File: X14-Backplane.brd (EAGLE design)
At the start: 160 x 100 mm, 28 parts, among them J2 PXC-PTSM-04-RA-1778641, J3 PXC-8-RA-1778683, J7 POE_TERMINAL

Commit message: X14-Backplane 11/29
This is the most up to date backplane as of 11/29/2021
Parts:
- removed C5: 47uF, Panasonic 47 uF cap - EEE-1CA470SP:PANASONIC_D
- removed J7: POE_TERMINAL, Dist_POE:CONN2_282834-2_TEC
- added J8: PXC-8-RA-1778683, Phoenix Contact PTSM 8 pin:PXC-8-RA-1778683
- added U$9: IPL_13X2, PI-SHIELD, Solenoid-Backplane:IPL13X2
- U$4: device CONN, Distribution-Backplane:IPL1-106-01-L-D-K(B-D) -> CONN, Distribution-Backplane:SAMTEC_IPL1-107-01-X-D-K(B-D)
- moved U$1 20.4 mm to (-100.3, 104.1), turned to 180 degrees
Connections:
- new net +3V3: U$9.1
- new net ALERT1: U$9.17
- new net ALERT2: U$9.19
- new net SOL1_1: J8.8, U$9.8
- new net SOL2_1: J8.7, U$9.10
- new net SOL3_1: J8.6, U$9.12
- new net SOL4_1: J8.5, U$9.14
- new net SOL5_1: J8.4, U$9.16
- new net SOL6_1: J8.3, U$9.18
- new net SWCLK: U$9.11
- new net SWDIO: U$9.13
- net 12V: now also J8.1, J8.2, U$4.07, U$9.2; no longer C5.+
- net 3V3: now also U$4.04; no longer U$4.4
- net 5V: now also U$4.01, U$4.02, U$4.03, U$9.3; no longer J7.1, U$4.1, U$4.2, U$4.3
- net ALERT_1: now also U$4.09; no longer U$4.8
- net ALERT_2: now also U$4.10; no longer U$4.9
- net C2_1: now also U$4.12, U$9.21; no longer U$4.11
- net C2_2: now also U$4.13, U$9.22; no longer U$4.12
- net CAN_H: now also U$9.24
- net CAN_L: now also U$9.26
- net CLK: now also U$4.11, U$9.23; no longer U$4.10
- net DATA: now also U$4.08, U$9.25; no longer U$4.7
- net GND: now also U$4.05, U$4.06, U$9.15, U$9.20, U$9.4, U$9.5, U$9.6, U$9.7, U$9.9; no longer C5.-, J7.2, U$4.5, U$4.6
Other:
- board size 160 x 100 mm -> 88.9 x 139.7 mm

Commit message: X14-Backplane 12/2
Most up to date backplane as of 12/2/2021
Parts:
- U$9: value IPL_13X2 -> 6X_CONN; device PI-SHIELD, Solenoid-Backplane:IPL13X2 -> PI-SHIELD, Solenoid-Backplane:IPL6X2
- moved R9 254.0 mm to (85.6, 28.7), turned to 180 degrees
- moved U$4 248.7 mm to (82.5, 123.4), turned to 270 degrees
- moved J8 246.2 mm to (86.1, 83.3), turned to 90 degrees
- moved U$5 245.0 mm to (95.2, 128.3), turned to 180 degrees
- moved J2 237.2 mm to (70.9, 50.8)
- moved J3 233.7 mm to (86.4, 59.2), turned to 90 degrees
- moved D4 232.9 mm to (85.6, 26.2), turned to 180 degrees
- moved D3 229.1 mm to (85.6, 23.4), turned to 180 degrees
- moved D2 225.6 mm to (85.6, 20.6), turned to 180 degrees
- moved R8 225.1 mm to (72.6, 54.9), turned to 90 degrees
- moved U$9 225.1 mm to (74.7, 88.1), turned to 90 degrees
- moved R7 224.3 mm to (75.4, 54.9), turned to 270 degrees
- moved H2 223.0 mm to (85.1, 3.81), flipped to the bottom
- moved D1 222.3 mm to (85.6, 17.8), turned to 180 degrees
- moved R5 215.2 mm to (26.7, 11.4), turned to 180 degrees
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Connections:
- removed net +3V3: U$9.1
- removed net ALERT1: U$9.17
- removed net ALERT2: U$9.19
- removed net GND: C4.2, J2.1, J3.1, J6.4, MUX.6, MUX.7, MUX.8, R1.1, R4.1, R5.1, U$1.10, U$2.10, U$3.10, U$4.05, U$4.06, U$8.1, U$9.15, U$9.20, U$9.4, U$9.5, U$9.6, U$9.7, U$9.9
- removed net SWCLK: U$9.11
- removed net SWDIO: U$9.13
- new net 12V_L: J8.1, J8.2, U$4.07, U$9.1, U$9.3
- new net GND_L: C4.2, J2.1, J3.1, J6.4, MUX.6, MUX.7, MUX.8, R1.1, R4.1, R5.1, U$1.10, U$2.10, U$3.10, U$4.14, U$8.1, U$9.5, U$9.9
- new net JH: U$4.05, U$4.06
- net 12V: no longer J8.1, J8.2, U$4.07, U$9.2
- net 3V3: now also U$9.11
- net 5V: now also U$9.7; no longer U$9.3
- net C2_1: no longer U$9.21
- net C2_2: no longer U$9.22
- net CAN_H: no longer U$9.24
- net CAN_L: no longer U$9.26
- net CLK: no longer U$9.23
- net DATA: no longer U$9.25
- net SOL1_1: now also J8.3, U$9.2; no longer J8.8, U$9.8
- net SOL2_1: now also J8.4, U$9.4; no longer J8.7, U$9.10
- net SOL3_1: now also J8.5, U$9.6; no longer J8.6, U$9.12
- net SOL4_1: now also J8.6, U$9.8; no longer J8.5, U$9.14
- net SOL5_1: now also J8.7, U$9.10; no longer J8.4, U$9.16
- net SOL6_1: now also J8.8, U$9.12; no longer J8.3, U$9.18
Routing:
- net CAN_L: track 0.00 -> 146.4 mm, vias 0 -> 2
- net CAN_H: track 0.00 -> 130.8 mm
- net SWCLK_3: track 0.00 -> 109.8 mm, vias 0 -> 1
- net SWDIO_3: track 0.00 -> 109.2 mm, vias 0 -> 1
- net NRST_3: track 0.00 -> 82.0 mm, vias 0 -> 1
- net SWCLK_2: track 0.00 -> 68.0 mm, vias 0 -> 1
- net SWDIO_2: track 0.00 -> 62.0 mm, vias 0 -> 1
- net 12V_L: track 0.00 -> 49.0 mm
- net C2_2: track 0.00 -> 29.8 mm
- net 5V: track 0.00 -> 28.1 mm
- net 3V3: track 0.00 -> 25.9 mm, vias 0 -> 2
- net C2_1: track 0.00 -> 25.8 mm
- net CLK: track 0.00 -> 21.8 mm
- net ALERT_2: track 0.00 -> 17.9 mm
- net PROG_1: track 0.00 -> 16.7 mm
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- added copper zone on layer 16, net 3V3
- added copper zone on layer 1, net 5V
- added copper zone on layer 1, net GND_L
- added copper zone on layer 16, net GND_L
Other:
- board size 88.9 x 139.7 mm -> 88.9 x 140.2 mm
- board text added: "Reserved Space for SMBUS->I2C Board"

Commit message: sfdgfhg
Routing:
- net NRST_3: track 82.0 -> 75.3 mm
- net SWDIO_2: track 62.0 -> 63.4 mm
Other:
- board text added: "Reserved Space for SMBUS->CAN Board"
- board text removed: "Reserved Space for SMBUS->I2C Board"
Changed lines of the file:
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@@
 <wire x1="38.862" y1="-0.508" x2="38.862" y2="1.016" width="0.1524" layer="46"/>
 <text x="67.818" y="123.952" size="1.016" layer="125">Reserved Space
-for SMBUS-&gt;I2C
+for SMBUS-&gt;CAN
 Board</text>
 </plain>
@@
 <contactref element="U$2" pad="9"/>
 <wire x1="20.78" y1="56.372" x2="20.78" y2="59.388" width="0.1524" layer="16"/>
-<wire x1="64.516" y1="72.136" x2="67.564" y2="75.184" width="0.1524" layer="16"/>
+<wire x1="65.532" y1="73.152" x2="67.564" y2="75.184" width="0.1524" layer="16"/>
 <via x="67.564" y="75.184" extent="1-16" drill="0.35"/>
-<wire x1="20.78" y1="59.388" x2="23.622" y2="62.23" width="0.1524" layer="16"/>
-<wire x1="23.622" y1="62.23" x2="61.722" y2="62.23" width="0.1524" layer="16"/>
-<wire x1="61.722" y1="62.23" x2="64.516" y2="65.024" width="0.1524" layer="16"/>
-<wire x1="64.516" y1="65.024" x2="64.516" y2="72.136" width="0.1524" layer="16"/>
+<wire x1="20.78" y1="59.388" x2="22.86" y2="61.468" width="0.1524" layer="16"/>
+<wire x1="22.86" y1="61.468" x2="63.246" y2="61.468" width="0.1524" layer="16"/>
+<wire x1="63.246" y1="61.468" x2="65.532" y2="63.754" width="0.1524" layer="16"/>
+<wire x1="65.532" y1="63.754" x2="65.532" y2="73.152" width="0.1524" layer="16"/>
 <wire x1="67.564" y1="75.184" x2="69.088" y2="75.184" width="0.1524" layer="1"/>
 </signal>
@@
 <contactref element="U$2" pad="11"/>
 <wire x1="22.78" y1="56.372" x2="22.78" y2="59.102" width="0.1524" layer="16"/>
-<wire x1="24.384" y1="60.706" x2="62.738" y2="60.706" width="0.1524" layer="16"/>
-<wire x1="62.738" y1="60.706" x2="66.04" y2="64.008" width="0.1524" layer="16"/>
-<wire x1="66.04" y1="64.008" x2="66.04" y2="72.644" width="0.1524" layer="16"/>
-<wire x1="66.04" y1="72.644" x2="67.056" y2="73.66" width="0.1524" layer="16"/>
+<wire x1="24.384" y1="60.706" x2="63.5" y2="60.706" width="0.1524" layer="16"/>
+<wire x1="63.5" y1="60.706" x2="66.294" y2="63.5" width="0.1524" layer="16"/>
+<wire x1="66.294" y1="63.5" x2="66.294" y2="72.898" width="0.1524" layer="16"/>
+<wire x1="66.294" y1="72.898" x2="67.056" y2="73.66" width="0.1524" layer="16"/>
 <wire x1="70.866" y1="73.66" x2="71.628" y2="74.422" width="0.1524" layer="16"/>
 <wire x1="71.628" y1="74.422" x2="71.628" y2="76.2" width="0.1524" layer="16"/>
@@
 <wire x1="22.78" y1="15.922" x2="24.384" y2="17.526" width="0.1524" layer="16"/>
 <wire x1="24.384" y1="17.526" x2="59.944" y2="17.526" width="0.1524" layer="16"/>
-<wire x1="61.976" y1="19.558" x2="61.976" y2="55.118" width="0.1524" layer="16"/>
+<wire x1="61.976" y1="19.558" x2="61.976" y2="56.642" width="0.1524" layer="16"/>
 <via x="75.692" y="77.978" extent="1-16" drill="0.35"/>
 <wire x1="75.692" y1="77.978" x2="75.692" y2="78.232" width="0.1524" layer="1"/>
 <wire x1="75.692" y1="78.232" x2="74.93" y2="78.994" width="0.1524" layer="1"/>
 <wire x1="74.93" y1="78.994" x2="73.768" y2="78.994" width="0.1524" layer="1"/>
-<wire x1="61.976" y1="55.118" x2="75.692" y2="68.834" width="0.1524" layer="16"/>
-<wire x1="75.692" y1="68.834" x2="75.692" y2="77.978" width="0.1524" layer="16"/>
+<wire x1="61.976" y1="56.642" x2="75.692" y2="70.358" width="0.1524" layer="16"/>
+<wire x1="75.692" y1="70.358" x2="75.692" y2="77.978" width="0.1524" layer="16"/>
 </signal>
 <signal name="CAN_H">
@@
 <contactref element="D3" pad="A"/>
 <contactref element="U$3" pad="6"/>
-<wire x1="16.78" y1="11.446" x2="16.78" y2="9.128" width="0.1524" layer="16"/>
-<wire x1="16.78" y1="9.128" x2="18.288" y2="7.62" width="0.1524" layer="16"/>
-<wire x1="18.288" y1="7.62" x2="66.294" y2="7.62" width="0.1524" layer="16"/>
-<wire x1="68.326" y1="9.652" x2="68.326" y2="18.034" width="0.1524" layer="16"/>
-<wire x1="68.326" y1="18.034" x2="73.66" y2="23.368" width="0.1524" layer="16"/>
-<wire x1="66.294" y1="7.62" x2="68.326" y2="9.652" width="0.1524" layer="16"/>
+<wire x1="16.78" y1="11.446" x2="16.78" y2="10.144" width="0.1524" layer="16"/>
+<wire x1="16.78" y1="10.144" x2="17.78" y2="9.144" width="0.1524" layer="16"/>
+<wire x1="17.78" y1="9.144" x2="59.436" y2="9.144" width="0.1524" layer="16"/>
+<wire x1="59.436" y1="9.144" x2="73.66" y2="23.368" width="0.1524" layer="16"/>
 <wire x1="73.66" y1="23.368" x2="78.232" y2="23.368" width="0.1524" layer="16"/>
 <via x="78.232" y="23.368" extent="1-16" drill="0.35"/>

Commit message: Revert "sfdgfhg"
This reverts commit 89fcb60d7aa2de489dc8c4b854d40a80c75a218c.
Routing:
- net NRST_3: track 75.3 -> 82.0 mm
- net SWDIO_2: track 63.4 -> 62.0 mm
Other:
- board text added: "Reserved Space for SMBUS->I2C Board"
- board text removed: "Reserved Space for SMBUS->CAN Board"
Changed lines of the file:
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@@
 <wire x1="38.862" y1="-0.508" x2="38.862" y2="1.016" width="0.1524" layer="46"/>
 <text x="67.818" y="123.952" size="1.016" layer="125">Reserved Space
-for SMBUS-&gt;CAN
+for SMBUS-&gt;I2C
 Board</text>
 </plain>
@@
 <contactref element="U$2" pad="9"/>
 <wire x1="20.78" y1="56.372" x2="20.78" y2="59.388" width="0.1524" layer="16"/>
-<wire x1="65.532" y1="73.152" x2="67.564" y2="75.184" width="0.1524" layer="16"/>
+<wire x1="64.516" y1="72.136" x2="67.564" y2="75.184" width="0.1524" layer="16"/>
 <via x="67.564" y="75.184" extent="1-16" drill="0.35"/>
-<wire x1="20.78" y1="59.388" x2="22.86" y2="61.468" width="0.1524" layer="16"/>
-<wire x1="22.86" y1="61.468" x2="63.246" y2="61.468" width="0.1524" layer="16"/>
-<wire x1="63.246" y1="61.468" x2="65.532" y2="63.754" width="0.1524" layer="16"/>
-<wire x1="65.532" y1="63.754" x2="65.532" y2="73.152" width="0.1524" layer="16"/>
+<wire x1="20.78" y1="59.388" x2="23.622" y2="62.23" width="0.1524" layer="16"/>
+<wire x1="23.622" y1="62.23" x2="61.722" y2="62.23" width="0.1524" layer="16"/>
+<wire x1="61.722" y1="62.23" x2="64.516" y2="65.024" width="0.1524" layer="16"/>
+<wire x1="64.516" y1="65.024" x2="64.516" y2="72.136" width="0.1524" layer="16"/>
 <wire x1="67.564" y1="75.184" x2="69.088" y2="75.184" width="0.1524" layer="1"/>
 </signal>
@@
 <contactref element="U$2" pad="11"/>
 <wire x1="22.78" y1="56.372" x2="22.78" y2="59.102" width="0.1524" layer="16"/>
-<wire x1="24.384" y1="60.706" x2="63.5" y2="60.706" width="0.1524" layer="16"/>
-<wire x1="63.5" y1="60.706" x2="66.294" y2="63.5" width="0.1524" layer="16"/>
-<wire x1="66.294" y1="63.5" x2="66.294" y2="72.898" width="0.1524" layer="16"/>
-<wire x1="66.294" y1="72.898" x2="67.056" y2="73.66" width="0.1524" layer="16"/>
+<wire x1="24.384" y1="60.706" x2="62.738" y2="60.706" width="0.1524" layer="16"/>
+<wire x1="62.738" y1="60.706" x2="66.04" y2="64.008" width="0.1524" layer="16"/>
+<wire x1="66.04" y1="64.008" x2="66.04" y2="72.644" width="0.1524" layer="16"/>
+<wire x1="66.04" y1="72.644" x2="67.056" y2="73.66" width="0.1524" layer="16"/>
 <wire x1="70.866" y1="73.66" x2="71.628" y2="74.422" width="0.1524" layer="16"/>
 <wire x1="71.628" y1="74.422" x2="71.628" y2="76.2" width="0.1524" layer="16"/>
@@
 <wire x1="22.78" y1="15.922" x2="24.384" y2="17.526" width="0.1524" layer="16"/>
 <wire x1="24.384" y1="17.526" x2="59.944" y2="17.526" width="0.1524" layer="16"/>
-<wire x1="61.976" y1="19.558" x2="61.976" y2="56.642" width="0.1524" layer="16"/>
+<wire x1="61.976" y1="19.558" x2="61.976" y2="55.118" width="0.1524" layer="16"/>
 <via x="75.692" y="77.978" extent="1-16" drill="0.35"/>
 <wire x1="75.692" y1="77.978" x2="75.692" y2="78.232" width="0.1524" layer="1"/>
 <wire x1="75.692" y1="78.232" x2="74.93" y2="78.994" width="0.1524" layer="1"/>
 <wire x1="74.93" y1="78.994" x2="73.768" y2="78.994" width="0.1524" layer="1"/>
-<wire x1="61.976" y1="56.642" x2="75.692" y2="70.358" width="0.1524" layer="16"/>
-<wire x1="75.692" y1="70.358" x2="75.692" y2="77.978" width="0.1524" layer="16"/>
+<wire x1="61.976" y1="55.118" x2="75.692" y2="68.834" width="0.1524" layer="16"/>
+<wire x1="75.692" y1="68.834" x2="75.692" y2="77.978" width="0.1524" layer="16"/>
 </signal>
 <signal name="CAN_H">
@@
 <contactref element="D3" pad="A"/>
 <contactref element="U$3" pad="6"/>
-<wire x1="16.78" y1="11.446" x2="16.78" y2="10.144" width="0.1524" layer="16"/>
-<wire x1="16.78" y1="10.144" x2="17.78" y2="9.144" width="0.1524" layer="16"/>
-<wire x1="17.78" y1="9.144" x2="59.436" y2="9.144" width="0.1524" layer="16"/>
-<wire x1="59.436" y1="9.144" x2="73.66" y2="23.368" width="0.1524" layer="16"/>
+<wire x1="16.78" y1="11.446" x2="16.78" y2="9.128" width="0.1524" layer="16"/>
+<wire x1="16.78" y1="9.128" x2="18.288" y2="7.62" width="0.1524" layer="16"/>
+<wire x1="18.288" y1="7.62" x2="66.294" y2="7.62" width="0.1524" layer="16"/>
+<wire x1="68.326" y1="9.652" x2="68.326" y2="18.034" width="0.1524" layer="16"/>
+<wire x1="68.326" y1="18.034" x2="73.66" y2="23.368" width="0.1524" layer="16"/>
+<wire x1="66.294" y1="7.62" x2="68.326" y2="9.652" width="0.1524" layer="16"/>
 <wire x1="73.66" y1="23.368" x2="78.232" y2="23.368" width="0.1524" layer="16"/>
 <via x="78.232" y="23.368" extent="1-16" drill="0.35"/>

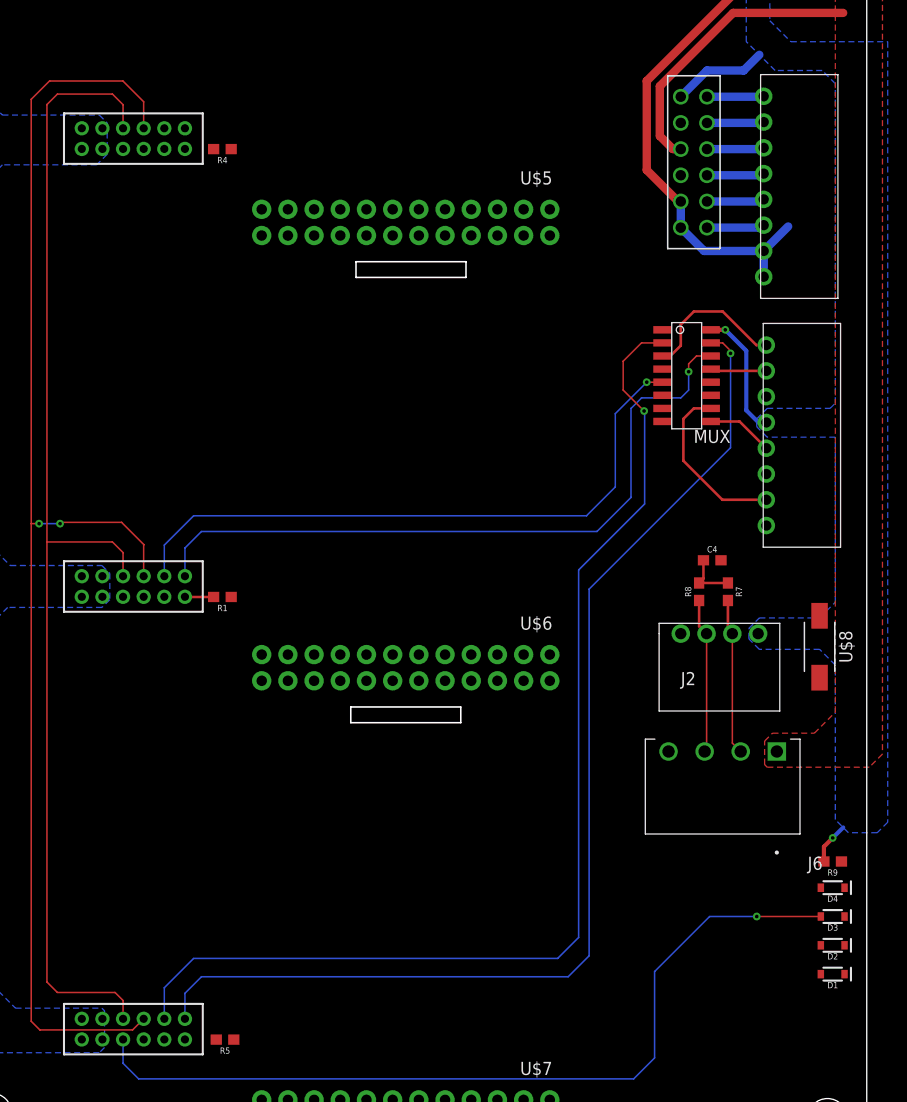
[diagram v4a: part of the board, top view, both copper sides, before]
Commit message: X14-Backplane 12/2 #2
This has more signals routed except from those from dist (top right of board) and the power between the ESC's
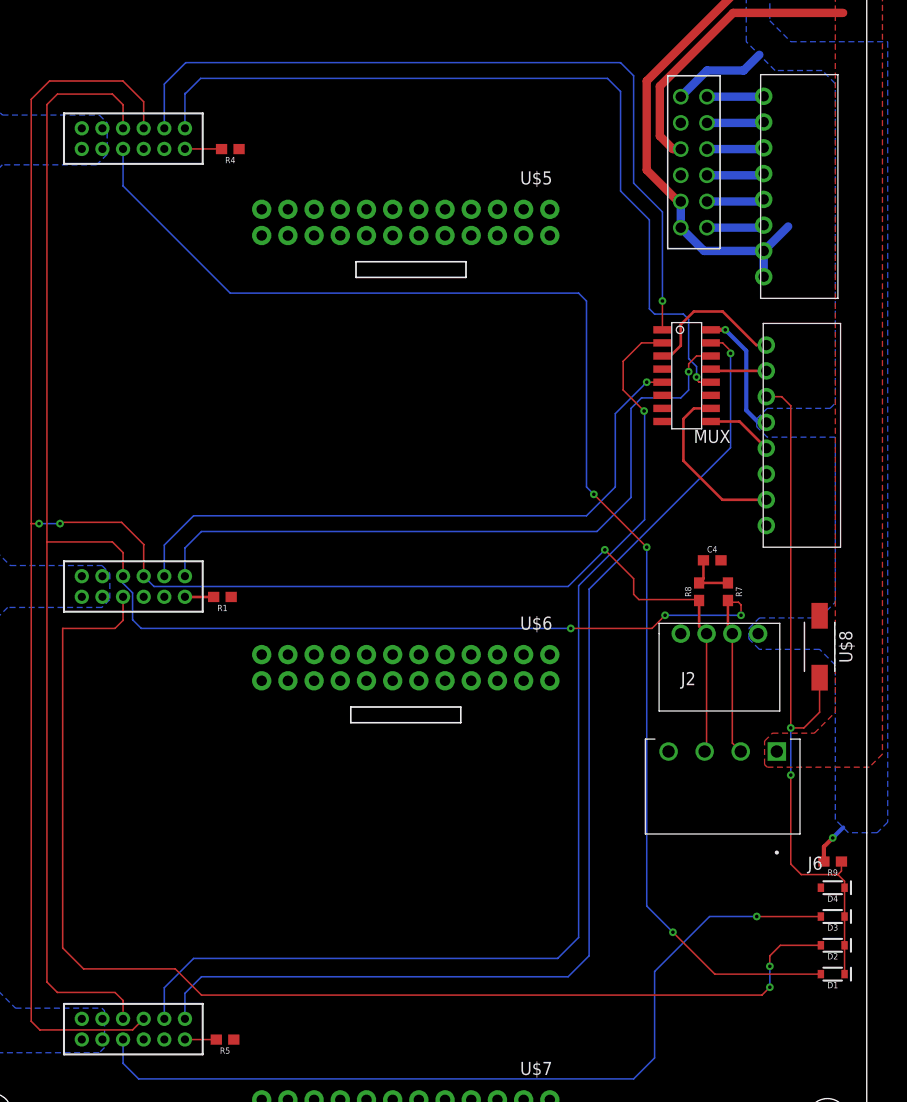
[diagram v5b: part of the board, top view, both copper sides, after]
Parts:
- moved R4 0.76 mm to (27.2, 97.8)
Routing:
- net NRST_1: track 0.00 -> 133.9 mm, vias 0 -> 3
- net NRST_2: track 0.00 -> 118.7 mm, vias 0 -> 2
- net SWCLK_1: track 0.00 -> 80.9 mm, vias 0 -> 1
- net SWDIO_1: track 0.00 -> 77.0 mm, vias 0 -> 1
- net NRST: track 0.00 -> 70.3 mm, vias 0 -> 2
- net CAN_H: track 130.8 -> 197.6 mm, vias 0 -> 3
- net CAN_L: track 146.4 -> 205.0 mm, vias 2 -> 3
- net ESCID_1: track 0.00 -> 3.55 mm
- net ESCID_3: track 0.00 -> 3.05 mm

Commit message: X14-Backplane 12/4
This is the most up to date version as of 12/4/2021
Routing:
- added copper zone on layer 1, net 12V
- added copper zone on layer 1, net 12VGND

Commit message: routing
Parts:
- removed J6: (no value), te 3.5m mm horiz 4 pin:TE_284512-4
- moved R4 6.25 mm to (21.6, 95.0), turned to 0 degrees
- moved R5 6.15 mm to (21.8, 7.62), turned to 0 degrees
- moved R1 6.12 mm to (21.8, 50.3), turned to 0 degrees
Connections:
- net 5V: no longer J6.1
- net CAN_H: no longer J6.2
- net CAN_L: no longer J6.3
- net GND_L: no longer J6.4
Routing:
- net 12V: track 0.00 -> 126.5 mm, vias 0 -> 30
- net 12VGND: track 0.00 -> 125.7 mm, vias 0 -> 27
- net GND_L: track 0.00 -> 19.4 mm, vias 0 -> 3
- net NRST_2: track 118.7 -> 131.9 mm
- net CAN_H: track 197.6 -> 185.8 mm
- net CAN_L: track 205.0 -> 193.5 mm
- net NRST_3: track 82.0 -> 76.2 mm
- net NRST_1: track 133.9 -> 135.8 mm
- net ESCID_2: track 2.79 -> 4.09 mm
- net 5V: track 28.1 -> 27.2 mm
- net ESCID_3: track 3.05 -> 3.83 mm
- net PROG_1: track 16.7 -> 16.0 mm
- net ESCID_1: track 3.55 -> 3.03 mm
- added copper zone on layer 16, net 12V
- added copper zone on layer 16, net 12VGND
- added copper zone on layer 16, net NICE
- added copper zone on layer 16, net WELOVEDESIGNREVIEWS

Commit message: rerouted board
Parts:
- U$9: value 6X_CONN -> 7X_CONN; device PI-SHIELD, Solenoid-Backplane:IPL6X2 -> PI-SHIELD, Solenoid-Backplane:IPL7X2
- moved D1 116.5 mm to (13.5, 109.2), turned to 0 degrees
- moved J3 108.3 mm to (0.51, 125.2), turned to 270 degrees
- moved D4 106.7 mm to (8.89, 100.3), turned to 0 degrees
- moved R9 102.1 mm to (3.56, 89.4), turned to 270 degrees
- moved U$8 93.7 mm to (3.56, 97.0)
- moved D2 85.6 mm to (13.0, 65.8), turned to 0 degrees
- moved D3 72.7 mm to (13.0, 22.4), turned to 0 degrees
- moved R7 64.0 mm to (12.2, 45.2), turned to 180 degrees
- moved J2 63.3 mm to (7.62, 49.8), turned to 270 degrees
- moved R8 60.8 mm to (12.2, 48.0), turned to 0 degrees
- moved C4 59.5 mm to (15.5, 46.7)
- moved MUX 58.0 mm to (23.9, 116.6), turned to 180 degrees
- moved U$9 51.9 mm to (80.8, 36.6), turned to 270 degrees
- moved J8 20.5 mm to (88.6, 63.0)
- moved U$7 10.9 mm to (94.5, 52.8)
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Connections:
- removed net JH: U$4.05, U$4.06
- new net 12L_GND: U$4.14, U$9.5
- net CAN_H: now also U$9.14
- net CAN_L: now also U$9.13
- net GND_L: now also U$4.05, U$4.06; no longer U$4.14, U$9.5
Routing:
- net 3V3: track 25.9 -> 394.4 mm, vias 2 -> 5
- net NRST_1: track 135.8 -> 2.17 mm, vias 3 -> 0
- net NRST_2: track 131.9 -> 2.43 mm, vias 2 -> 0
- net 12L_GND: track 0.00 -> 109.2 mm
- net NRST_3: track 76.2 -> 2.43 mm, vias 1 -> 0
- net 5V: track 27.2 -> 92.4 mm
- net SOL6_1: track 5.52 -> 67.7 mm
- net SWDIO_1: track 77.0 -> 17.9 mm, vias 1 -> 0
- net 12V_L: track 49.0 -> 107.6 mm
- net SWCLK_1: track 80.9 -> 24.6 mm, vias 1 -> 2
- net SOL5_1: track 5.53 -> 61.6 mm
- net SOL4_1: track 5.55 -> 55.5 mm
- net SOL3_1: track 5.66 -> 49.4 mm
- net CAN_H: track 185.8 -> 224.0 mm, vias 3 -> 5
- net NRST: track 70.3 -> 108.2 mm, vias 2 -> 4
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- added copper zone on layer 1, net 3V3
- added copper zone on layer 16, net 5V
- removed copper zone on layer 16, net 3V3
- removed copper zone on layer 1, net 5V
- removed copper zone on layer 16, net NICE
- removed copper zone on layer 16, net WELOVEDESIGNREVIEWS
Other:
- board size 88.9 x 140.2 mm -> 88.9 x 139.7 mm
